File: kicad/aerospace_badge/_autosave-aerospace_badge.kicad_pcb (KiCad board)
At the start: 2 copper layers, 134.3 x 140 mm, 20 parts, among them J1 Conn_01x02, J2 Conn_01x02, J3 Conn_02x03_Counter_Clockwise, J4 Conn_01x04, J6 Conn_01x01_Male, J7 Conn_01x01_Male, J8 Conn_01x01_Male, SW1 SW_SPDT, U1 ATtiny85-20SU

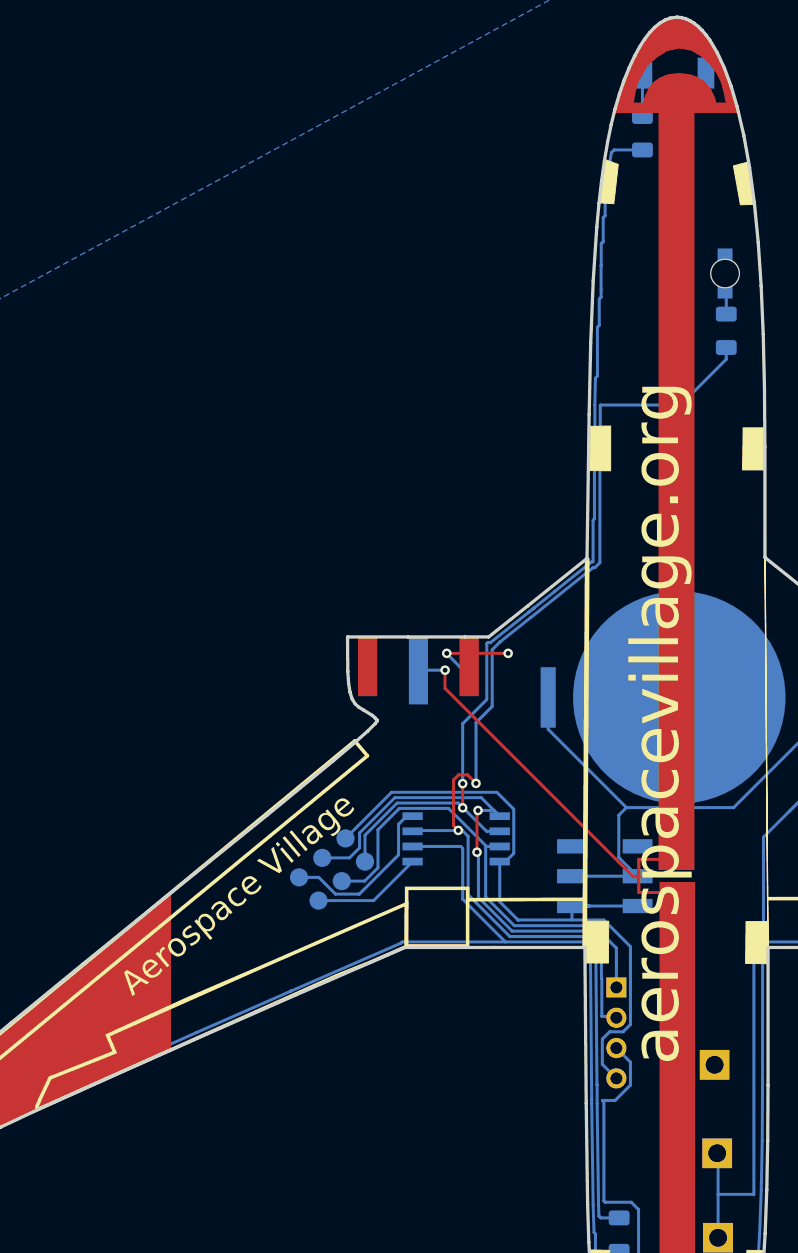
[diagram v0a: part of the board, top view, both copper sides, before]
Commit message: updated, needs another check prior to fabrication.
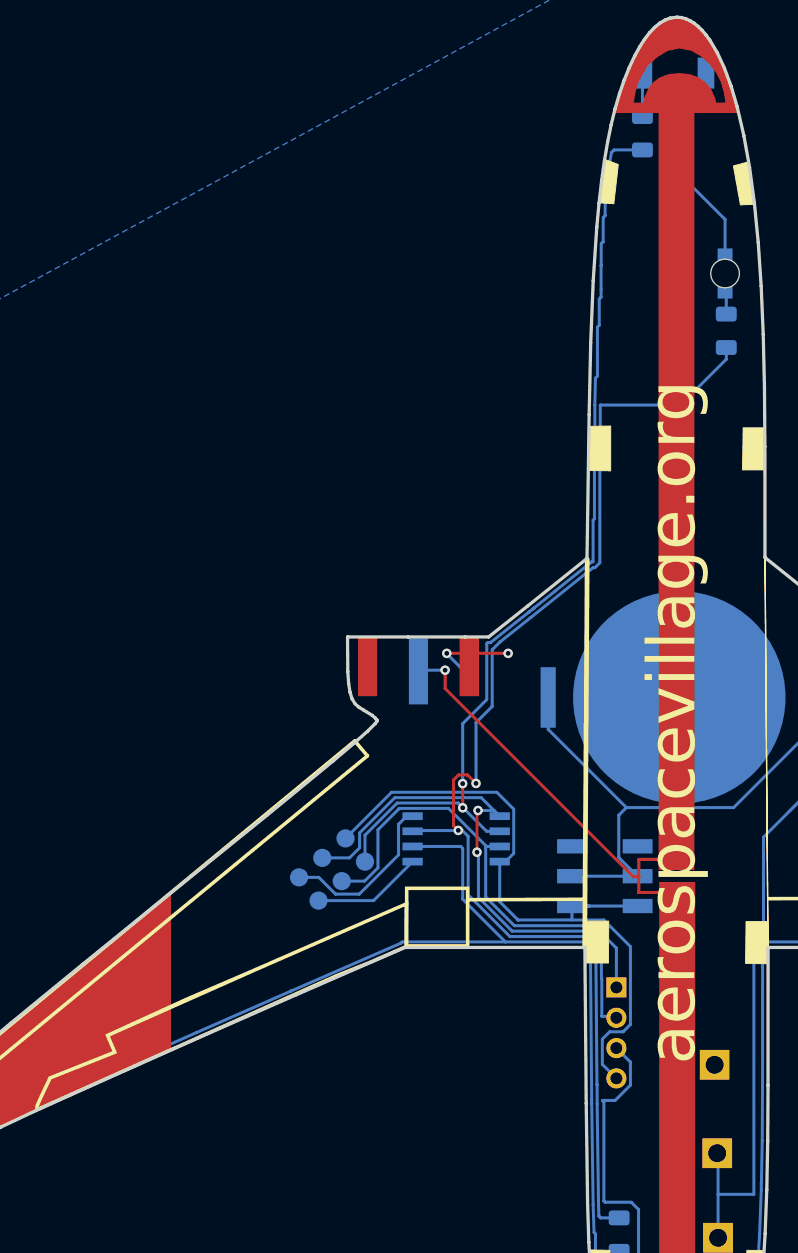
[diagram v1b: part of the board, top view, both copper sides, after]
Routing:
- net GND: track 74.0 -> 93.0 mm
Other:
- board text added: "captechu.edu"
- board text removed: "Aerospace Village"
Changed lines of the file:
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@@
     (thickness 1.6)
     (drawings 13)
-    (tracks 386)
+    (tracks 392)
     (zones 0)
     (modules 20)
@@
   )
   (layers
-    (0 F.Cu signal)
+    (0 F.Cu signal hide)
     (31 B.Cu signal)
     (32 B.Adhes user hide)
@@
     (34 B.Paste user hide)
     (35 F.Paste user hide)
-    (36 B.SilkS user)
+    (36 B.SilkS user hide)
     (37 F.SilkS user)
     (38 B.Mask user hide)
-    (39 F.Mask user hide)
+    (39 F.Mask user)
     (40 Dwgs.User user hide)
     (41 Cmts.User user hide)
@@
     (add_net "Net-(SW1-Pad1)")
     (add_net VCC)
-  )
-  (module aerospace_badge:wire_terminal_sr99s01 (layer F.Cu)
-    (at 151.5618 116.7638 90)
-    (fp_text reference J7 (at 3.6576 -2.5908 90) (layer B.SilkS)
-      (effects (font (size 1 1) (thickness 0.15)) (justify mirror))
-    )
-    (fp_text value Conn_01x01_Male (at 5.5753 -2.47142 90) (layer F.Fab)
-      (effects (font (size 1 1) (thickness 0.15)))
-    )
-    (pad "" thru_hole rect (at 7.5 0 90) (size 2.5 2.5) (drill 1.5) (layers *.Cu *.Mask))
-    (pad 1 thru_hole rect (at 0.0889 0.2159 90) (size 2.5 2.5) (drill 1.5) (layers *.Cu *.Mask)
-      (net 9 "Net-(J2-Pad1)"))
-  )
-  (module aerospace_badge:wire_terminal_sr99s01 (layer F.Cu)
-    (at 152.019 123.6218 270)
-    (fp_text reference J6 (at 4.0075 2.9718 90) (layer B.SilkS)
-      (effects (font (size 1 1) (thickness 0.15)) (justify mirror))
-    )
-    (fp_text value Conn_01x01_Male (at 5.5753 -2.47142 90) (layer F.Fab)
-      (effects (font (size 1 1) (thickness 0.15)))
-    )
-    (pad 1 thru_hole rect (at 0.134 0.1651 270) (size 2.5 2.5) (drill 1.5) (layers *.Cu *.Mask)
-      (net 9 "Net-(J2-Pad1)"))
-    (pad "" thru_hole rect (at 7.5 0 270) (size 2.5 2.5) (drill 1.5) (layers *.Cu *.Mask))
-  )
-  (module aerospace_badge:switch_JS202011SCQN (layer B.Cu)
-    (at 142.3602 93.4612 270)
-    (fp_text reference SW1 (at 0.44196 -5.04952 270) (layer B.SilkS)
-      (effects (font (size 1 1) (thickness 0.15)) (justify mirror))
-    )
-    (fp_text value SW_SPDT (at 0.06858 5.16382 270) (layer B.Fab)
-      (effects (font (size 1 1) (thickness 0.15)) (justify mirror))
-    )
-    (pad 1 smd rect (at -2.5 -2.75 270) (size 1.2 2.5) (layers B.Cu B.Paste B.Mask)
-      (net 17 "Net-(SW1-Pad1)"))
-    (pad 2 smd rect (at 0 -2.75 270) (size 1.2 2.5) (layers B.Cu B.Paste B.Mask)
-      (net 12 "Net-(BT1-Pad1)"))
-    (pad 3 smd rect (at 2.5 -2.75 270) (size 1.2 2.5) (layers B.Cu B.Paste B.Mask)
-      (net 2 VCC))
-    (pad 1 smd rect (at -2.5 2.75 270) (size 1.2 2.5) (layers B.Cu B.Paste B.Mask)
-      (net 17 "Net-(SW1-Pad1)"))
-    (pad 2 smd rect (at 0 2.75 270) (size 1.2 2.5) (layers B.Cu B.Paste B.Mask)
-      (net 12 "Net-(BT1-Pad1)"))
-    (pad 3 smd rect (at 2.5 2.75 270) (size 1.2 2.5) (layers B.Cu B.Paste B.Mask)
-      (net 2 VCC))
   )
   (module aerospace_badge:badge_v02 (layer F.Cu)
@@
     (fp_poly (pts (xy -63.597274 24.956122) (xy -62.760004 23.958304) (xy -62.227833 24.404848) (xy -63.065103 25.402667)
       (xy -63.597274 24.956122)) (layer F.Mask) (width 0))
-    (fp_poly (pts (xy -3.27911 -63.753463) (xy -3.034272 -64.567835) (xy -2.275991 -65.91572) (xy -1.438792 -66.646287)
-      (xy -0.60706 -67.1576) (xy 0.384292 -67.36489) (xy 1.386873 -67.169973) (xy 2.241601 -66.668052)
-      (xy 2.939126 -66.000248) (xy 3.470102 -65.307682) (xy 3.842108 -64.549667) (xy 4.08256 -63.737314)
-      (xy 4.250432 -62.824852) (xy 3.470102 -62.824852) (xy 3.383592 -63.209285) (xy 2.982261 -64.056909)
-      (xy 2.597065 -64.511133) (xy 2.053397 -64.909212) (xy 1.324668 -65.193833) (xy 0.38429 -65.307682)
-      (xy -0.553873 -65.208162) (xy -1.276781 -64.930267) (xy -1.812225 -64.533064) (xy -2.187995 -64.075624)
-      (xy -2.571681 -63.216304) (xy -2.650171 -62.824853) (xy -3.446369 -62.824853) (xy -3.27911 -63.753463)) (layer F.Mask) (width 0.070004))
+    (fp_poly (pts (xy -3.527877 -63.775041) (xy -3.283039 -64.589413) (xy -2.524758 -65.937298) (xy -1.687559 -66.667865)
+      (xy -0.855827 -67.179178) (xy 0.135525 -67.386468) (xy 1.138106 -67.191551) (xy 1.992834 -66.68963)
+      (xy 2.690359 -66.021826) (xy 3.221335 -65.32926) (xy 3.593341 -64.571245) (xy 3.833793 -63.758892)
+      (xy 4.001665 -62.84643) (xy 3.221335 -62.84643) (xy 3.134825 -63.230863) (xy 2.733494 -64.078487)
+      (xy 2.348298 -64.532711) (xy 1.80463 -64.93079) (xy 1.075901 -65.215411) (xy 0.135523 -65.32926)
+      (xy -0.80264 -65.22974) (xy -1.525548 -64.951845) (xy -2.060992 -64.554642) (xy -2.436762 -64.097202)
+      (xy -2.820448 -63.237882) (xy -2.898938 -62.846431) (xy -3.695136 -62.846431) (xy -3.527877 -63.775041)) (layer F.Mask) (width 0.070004))
     (fp_line (start -0.484987 -69.919165) (end -0.92066 -69.752044) (layer Edge.Cuts) (width 0.273381))
     (fp_line (start -0.92066 -69.752044) (end -1.354227 -69.491805) (layer Edge.Cuts) (width 0.273381))
@@
       (net 8 "Net-(J1-Pad1)"))
   )
+  (module aerospace_badge:wire_terminal_sr99s01 (layer F.Cu)
+    (at 151.5618 116.7638 90)
+    (fp_text reference J7 (at 3.683 2.5527 90) (layer B.SilkS)
+      (effects (font (size 1 1) (thickness 0.15)) (justify mirror))
+    )
+    (fp_text value Conn_01x01_Male (at 5.5753 -2.47142 90) (layer F.Fab)
+      (effects (font (size 1 1) (thickness 0.15)))
+    )
+    (pad "" thru_hole rect (at 7.5 0 90) (size 2.5 2.5) (drill 1.5) (layers *.Cu *.Mask))
+    (pad 1 thru_hole rect (at 0.0889 0.2159 90) (size 2.5 2.5) (drill 1.5) (layers *.Cu *.Mask)
+      (net 9 "Net-(J2-Pad1)"))
+  )
+  (module aerospace_badge:wire_terminal_sr99s01 (layer F.Cu)
+    (at 152.019 123.6218 270)
+    (fp_text reference J6 (at 3.6449 -2.2987 90) (layer B.SilkS)
+      (effects (font (size 1 1) (thickness 0.15)) (justify mirror))
+    )
+    (fp_text value Conn_01x01_Male (at 5.5753 -2.47142 90) (layer F.Fab)
+      (effects (font (size 1 1) (thickness 0.15)))
+    )
+    (pad 1 thru_hole rect (at 0.134 0.1651 270) (size 2.5 2.5) (drill 1.5) (layers *.Cu *.Mask)
+      (net 9 "Net-(J2-Pad1)"))
+    (pad "" thru_hole rect (at 7.5 0 270) (size 2.5 2.5) (drill 1.5) (layers *.Cu *.Mask))
+  )
+  (module aerospace_badge:switch_JS202011SCQN (layer B.Cu)
+    (at 142.3602 93.4612 270)
+    (fp_text reference SW1 (at 0.44196 -5.04952 270) (layer B.SilkS)
+      (effects (font (size 1 1) (thickness 0.15)) (justify mirror))
+    )
+    (fp_text value SW_SPDT (at 0.06858 5.16382 270) (layer B.Fab)
+      (effects (font (size 1 1) (thickness 0.15)) (justify mirror))
+    )
+    (pad 1 smd rect (at -2.5 -2.75 270) (size 1.2 2.5) (layers B.Cu B.Paste B.Mask)
+      (net 17 "Net-(SW1-Pad1)"))
+    (pad 2 smd rect (at 0 -2.75 270) (size 1.2 2.5) (layers B.Cu B.Paste B.Mask)
+      (net 12 "Net-(BT1-Pad1)"))
+    (pad 3 smd rect (at 2.5 -2.75 270) (size 1.2 2.5) (layers B.Cu B.Paste B.Mask)
+      (net 2 VCC))
+    (pad 1 smd rect (at -2.5 2.75 270) (size 1.2 2.5) (layers B.Cu B.Paste B.Mask)
+      (net 17 "Net-(SW1-Pad1)"))
+    (pad 2 smd rect (at 0 2.75 270) (size 1.2 2.5) (layers B.Cu B.Paste B.Mask)
+      (net 12 "Net-(BT1-Pad1)"))
+    (pad 3 smd rect (at 2.5 2.75 270) (size 1.2 2.5) (layers B.Cu B.Paste B.Mask)
+      (net 2 VCC))
+  )
   (module sunled:XZMYK45WT-9 (layer B.Cu)
     (at 148.2379 26.1747 180)
-    (fp_text reference D1 (at 5.10286 0.32512 90) (layer B.SilkS)
+    (fp_text reference D1 (at -1.8253 2.5146 90) (layer B.SilkS)
       (effects (font (size 1 1) (thickness 0.15)) (justify mirror))
     )
@@
       (net 1 GND))
   )
+  (gr_text captechu.edu (at 184.5183 97.8408 330) (layer B.SilkS)
+    (effects (font (size 3 3) (thickness 0.5)) (justify mirror))
+  )
   (gr_text OFF (at 142.1638 88.6714) (layer B.SilkS)
     (effects (font (size 1.5 1.5) (thickness 0.3)) (justify mirror))
@@
     (effects (font (size 0.5 0.5) (thickness 0.125)) (justify mirror))
   )
-  (gr_text JLCJLCJLCJLC (at 148.4249 88.4809) (layer B.SilkS)
+  (gr_text JLCJLCJLCJLC (at 148.5519 68.7832) (layer B.SilkS)
     (effects (font (size 1 1) (thickness 0.15)) (justify mirror))
   )
-  (gr_text aerospacevillage.org (at 146.6469 80.6196 90) (layer F.SilkS)
+  (gr_text aerospacevillage.org (at 148.0058 80.5688 90) (layer F.SilkS)
     (effects (font (size 4 4) (thickness 0.5)))
   )
   (gr_text v02 (at 128.8796 157.8864) (layer B.Cu)
     (effects (font (size 1.5 1.5) (thickness 0.3)) (justify mirror))
-  )
-  (gr_text "Aerospace Village" (at 111.5822 94.9452 40) (layer F.SilkS)
-    (effects (font (size 2 2) (thickness 0.3)))
   )
   (gr_text ISP (at 123.1011 89.5096 310) (layer B.SilkS)
@@
   (segment (start 143.6624 130.8333) (end 143.6624 130.81) (width 0.254) (layer B.Cu) (net 1))
   (segment (start 145.189401 121.389601) (end 144.5768 120.777) (width 0.254) (layer B.Cu) (net 1))
+  (segment (start 152.4381 41.4062) (end 152.4381 38.4302) (width 0.25) (layer B.Cu) (net 1))
+  (segment (start 152.4381 38.4302) (end 147.2057 33.1978) (width 0.25) (layer B.Cu) (net 1))
+  (segment (start 147.2057 33.1978) (end 147.2057 30.1371) (width 0.25) (layer B.Cu) (net 1))
+  (segment (start 147.2057 30.1371) (end 147.1168 30.0482) (width 0.25) (layer B.Cu) (net 1))
+  (segment (start 147.1168 29.8958) (end 150.8379 26.1747) (width 0.25) (layer B.Cu) (net 1))
+  (segment (start 147.1168 30.0482) (end 147.1168 29.8958) (width 0.25) (layer B.Cu) (net 1))
   (segment (start 139.6102 95.9612) (end 145.1102 95.9612) (width 0.254) (layer B.Cu) (net 2))
   (segment (start 134.733301 87.845099) (end 134.733301 91.555101) (width 0.25) (layer B.Cu) (net 2))
@@
     (polygon
       (pts
-        (xy 149.73935 26.723975) (xy 146.83105 26.641425) (xy 146.6469 24.2824) (xy 148.41855 23.61565) (xy 149.82825 24.41575)
+        (xy 149.89175 26.292175) (xy 146.98345 26.209625) (xy 146.6977 24.892) (xy 148.209 24.0919) (xy 149.8727 24.7015)
       )
     )
